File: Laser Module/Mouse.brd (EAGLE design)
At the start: 100 x 50 mm, 74 parts, among them Q2 2.5A/30V, U1 RFM69HCW, U10 74AHC1G125, U2 HALL-EFFECTSMD, U3 HALL-EFFECTSMD, U4 HALL-EFFECTSMD, U5 HALL-EFFECTSMD, U6 BQ27441-G1, U7 BQ24075, U8 ATSAMD21G-A, U9 3.3V, Y1 32.768kHz

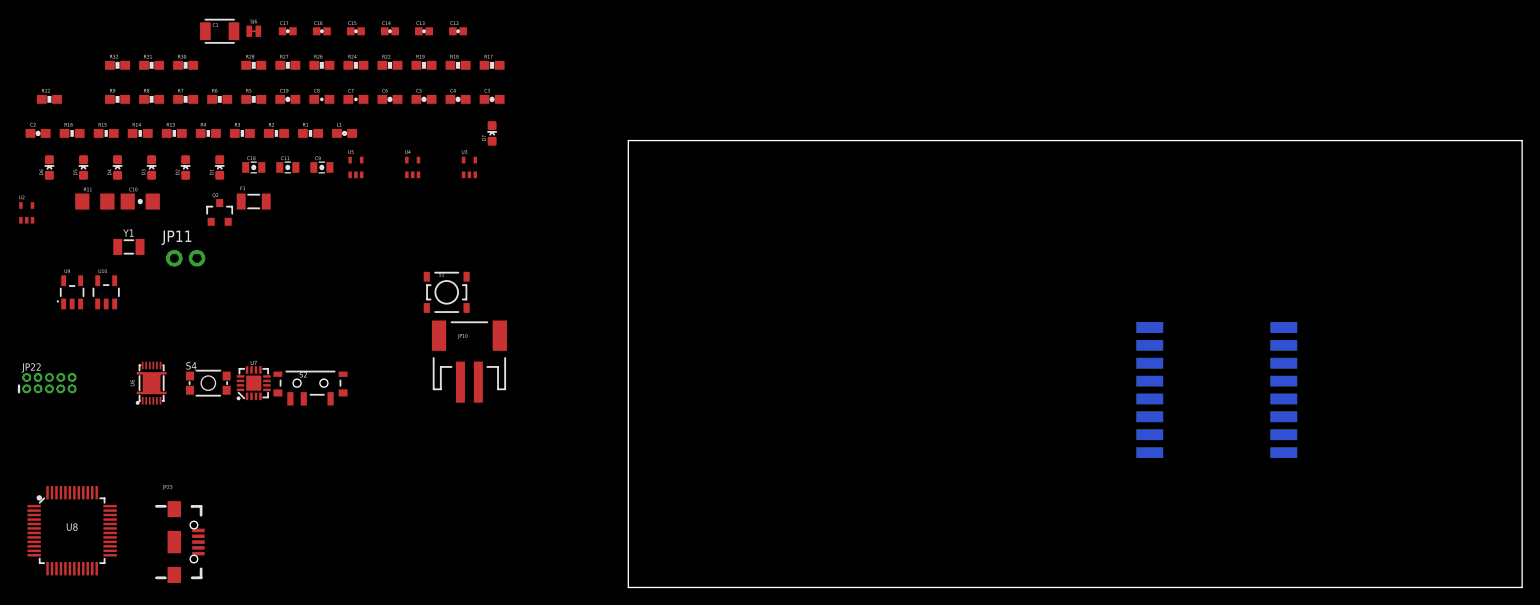
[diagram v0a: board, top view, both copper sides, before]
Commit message: Worked on the laser and dongle schematics Placed the parts on the laser and dongle boards in their rough locations
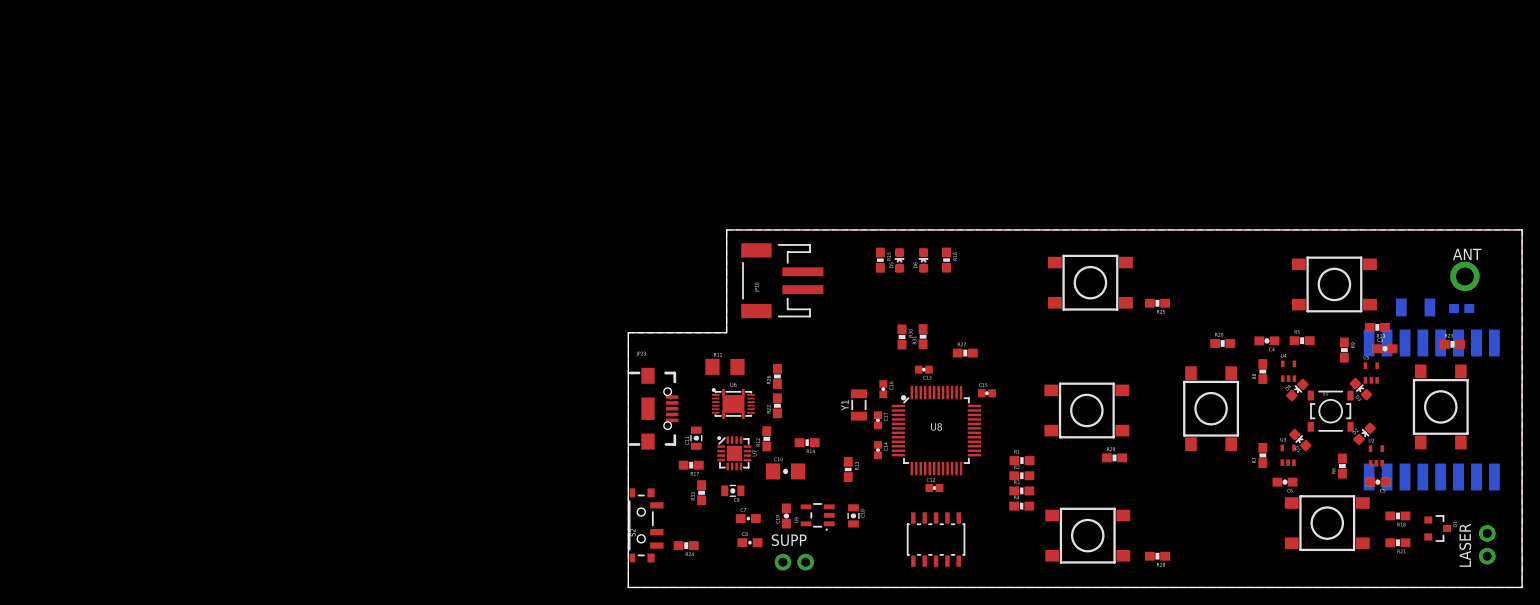
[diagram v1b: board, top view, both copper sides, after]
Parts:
- removed D7: RED, SparkFun-LED:LED-0603
- removed F1: 500mA, SparkFun-PowerIC:PTC-1206
- removed JP11: (no value), mike-temp:1X02_NO_SILK
- removed L1: FB - 30Ohm, SparkFun-Passives:0603
- removed Q2: 2.5A/30V, SparkFun-DiscreteSemi:SOT23-3
- removed R19: 10K, SparkFun-Resistors:0603-RES
- removed R32: 47K, SparkFun-Resistors:0603-RES
- removed SJ6: PWR-LED, SparkFun-Passives:PAD-JUMPER-2-NC_BY_TRACE_NO_SILK
- removed U10: 74AHC1G125, SparkFun-DigitalIC:SOT23-5
- added ANT: (no value), SparkFun-Connectors:1X01_2MM
- added LASER: (no value), SparkFun-Connectors:1X02_NO_SILK
- added Q1: MOSFET-NCHANNELAO3404A, SparkFun-DiscreteSemi:SOT23-3
- added R10, R20, R21, R23, R25, R29: 10k, SparkFun-Resistors:0603-RES
- added R33: 10K, SparkFun-Resistors:0603-RES
- added S3, S5, S6, S7, S8, S9: SWITCH-MOMENTARY-2SMD-4, SparkFun-Electromechanical:TACTILE_SWITCH_TALL
- added SUPP: (no value), mike-temp:1X02_NO_SILK
- JP22: value CORTEX_DEBUGPTH -> CORTEX_DEBUGSMD; device samd21-temp:2X5-PTH-1.27MM -> SparkFun-Connectors:SAMTECH_FTSH-105-01
- R18: value 10K -> 330
- R28: value 330 -> 10k
- S4: value RESET -> SWITCH-MOMENTARY-2SMD-4; device samd21-temp:TACTILE_SWITCH_SMD_4.6X2.8MM -> SparkFun-Electromechanical:TACTILE_SWITCH_TALL
- moved C2 160.5 mm to (93.2, 31.2), flipped to the bottom, turned to 180 degrees
- moved U2 153.4 mm to (83.7, 14.7)
- moved R9 140.1 mm to (80.1, 26.6), turned to 270 degrees
- moved D3 137.6 mm to (82.0, 22.2), turned to 45 degrees
- moved C1 137.3 mm to (88.1, 31.3), flipped to the bottom
- moved D2 135.2 mm to (82.4, 17.2), turned to 315 degrees
- moved D4 134.3 mm to (74.8, 22.1), turned to 315 degrees
- moved R6 132.1 mm to (79.9, 13.6), turned to 90 degrees
- moved R8 128.0 mm to (71.0, 24.2), turned to 90 degrees
- moved R7 126.9 mm to (71.0, 14.8), turned to 90 degrees
- moved D1 124.7 mm to (75.2, 16.5), turned to 45 degrees
- moved R5 120.4 mm to (75.4, 27.6)
- moved R18 116.6 mm to (86.1, 8.00), turned to 180 degrees
- moved U5 115.9 mm to (83.1, 24.0)
- moved R28 115.1 mm to (59.2, 3.50), turned to 180 degrees
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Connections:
- removed net A0: U8.3
- removed net A1: U8.7
- removed net A2: U8.8
- removed net A3: U8.9
- removed net AREF: U8.4
- removed net D0/RXI: U8.16
- removed net D1/TXO: U8.15
- removed net D10/SS: U8.27
- removed net D11/MOSI: U8.25
- removed net D12/MISO: U8.28
- removed net D13/SCK: U8.26
- removed net D2: U8.23
- removed net D3: U8.14
- removed net D4: U8.13
- removed net D5: U8.24
- removed net D6: U8.29
- removed net D7: U8.30
- removed net D8: U8.11
- removed net D9: U8.12
- removed net EN2: U7.5
- removed net N$14: D7.A, R28.1
- removed net N$18: F1.2, Q2.3
- removed net N$20: Q2.1, R32.1, U10.4
- removed net N$23: D7.C, SJ6.2
- removed net RF_NSS: U1.5
- removed net RX_LED: U8.48
- removed net SCL: U8.32
- removed net SDA: U8.31
- removed net TRK_BTN: R5.2, S1.1
- removed net TX_LED: U8.39
- new net DWN_BTN: R23.2, S6.A2, U8.15
- new net LFT_BTN: R10.2, S3.A2, U8.8
- new net LFT_MOUSE: R28.2, S8.A2, U8.21
- new net LSR_BTN: R25.2, S7.A2, U8.16
- new net LSR_OUT: R18.2, U8.9
- new net MDL_MOUSE: R5.2, S1.1, U8.11
- new net N$6: Q1.1, R18.1
- new net N$8: LASER.2, Q1.3
- new net RF_SS: U1.5, U8.27
- new net RHT_BTN: R21.2, S5.A2, U8.14
- new net RHT_MOUSE: R29.2, S9.A2, U8.22
- new net UP_BTN: R20.2, S4.A2, U8.13
- net !RESET: no longer S4.3, S4.4
- net 3.3V: now also S3.B2, S4.B2, S5.B2, S6.B2, S7.B2, S8.B2, S9.B2; no longer L1.1, R28.2
- net ANT: now also ANT.1
- net BLU_PWM: now also U8.23
- net BMS_SCL: now also U8.32
- net BMS_SDA: now also U8.31
- net EN1: now also R33.2; no longer R18.2
- net GND: now also Q1.2, R10.1, R20.1, R21.1, R23.1, R25.1, R28.1, R29.1, SUPP.2, U7.5; no longer JP11.2, R19.2, S4.1, S4.2, SJ6.1, U10.3
- net GPOUT: now also U8.10
- net GRN_PWM: now also U8.29
- net HALL_DWN: now also U8.47
- net HALL_LFT: now also U8.48
- net HALL_RHT: now also U8.7
- net HALL_UP: now also U8.12
- net N$19: no longer U10.1, U10.2
- net OUT: now also R33.1; no longer R18.1, R19.1
- net RED_PWM: now also U8.24
- net RF_MISO: now also U8.28
- net RF_MOSI: now also U8.25
- net RF_SCK: now also U8.26
- net VDDANA: no longer L1.2
- net VIN: no longer Q2.2, R32.2, U10.5
- net V_BATT: now also LASER.1
- net V_USB: now also SUPP.1; no longer F1.1, JP11.1
- net WHT_PWM: now also U8.30
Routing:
- added copper zone on layer 1, net GND
- added copper zone on layer 16, net GND
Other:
- board size 100 x 50 mm -> 100 x 40 mm

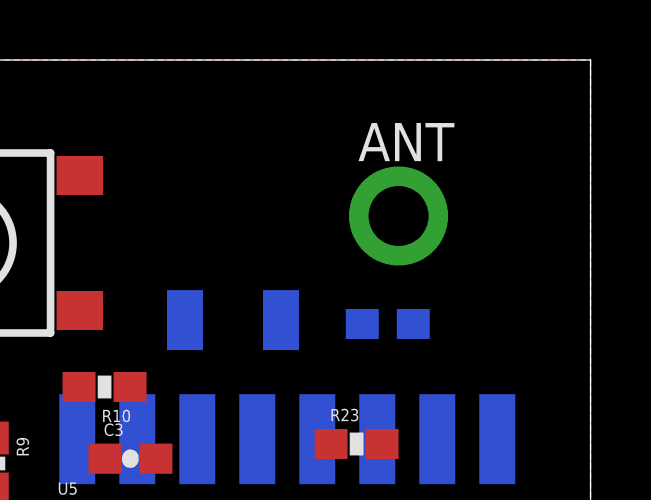
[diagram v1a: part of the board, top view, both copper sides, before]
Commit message: Created, placed, and routed a starter board for the Camera Module
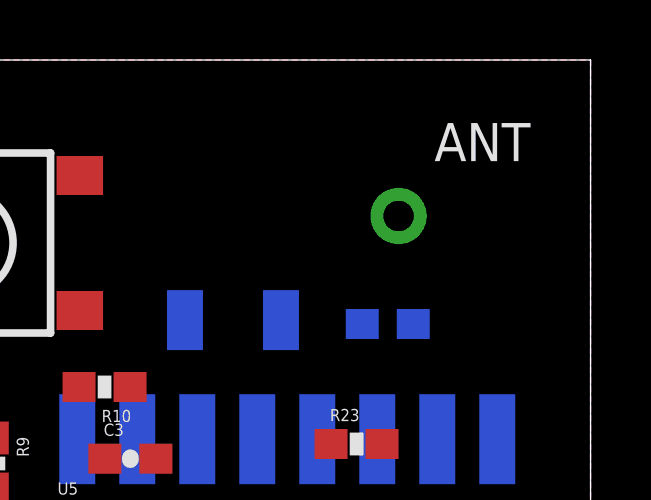
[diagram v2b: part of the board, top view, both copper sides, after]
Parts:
- ANT: device SparkFun-Connectors:1X01_2MM -> SparkFun-Connectors:1X01_NO_SILK
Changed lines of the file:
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@@
 <attribute name="PROD_ID" value="RES-00824" x="8.2" y="10.6" size="1.778" layer="27" rot="R90" display="off"/>
 </element>
-<element name="ANT" library="SparkFun-Connectors" package="1X01_2MM" value="" x="93.6" y="34.8"/>
+<element name="ANT" library="SparkFun-Connectors" package="1X01_NO_SILK" value="" x="93.6" y="34.8"/>
 <element name="Q1" library="SparkFun-DiscreteSemi" package="SOT23-3" value="MOSFET-NCHANNELAO3404A" x="90.5" y="6.6" smashed="yes" rot="R270">
 <attribute name="PROD_ID" value="TRAN-12988" x="90.5" y="6.6" size="1.778" layer="27" rot="R270" display="off"/>

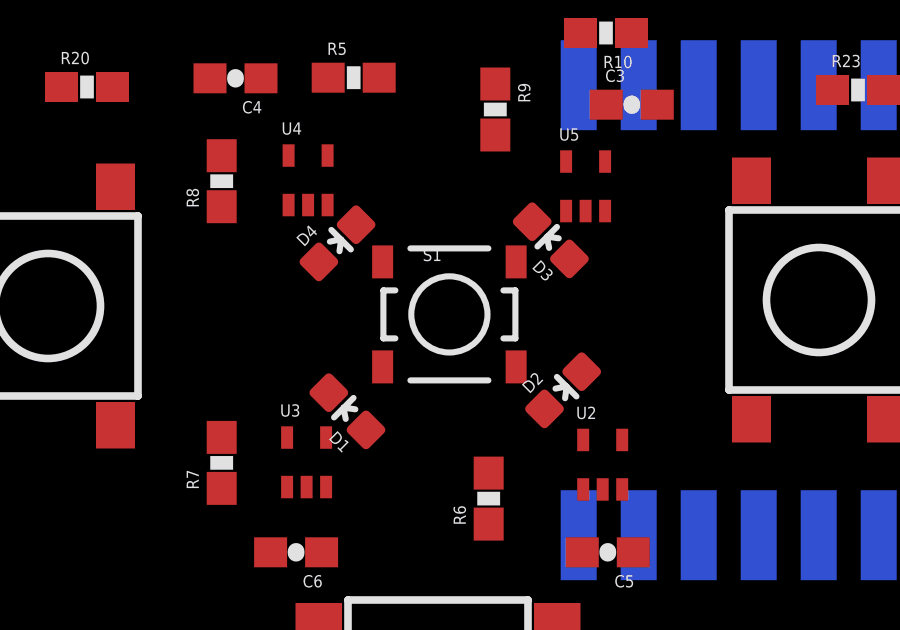
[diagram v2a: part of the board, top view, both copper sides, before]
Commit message: Routed the dongle and camera modules
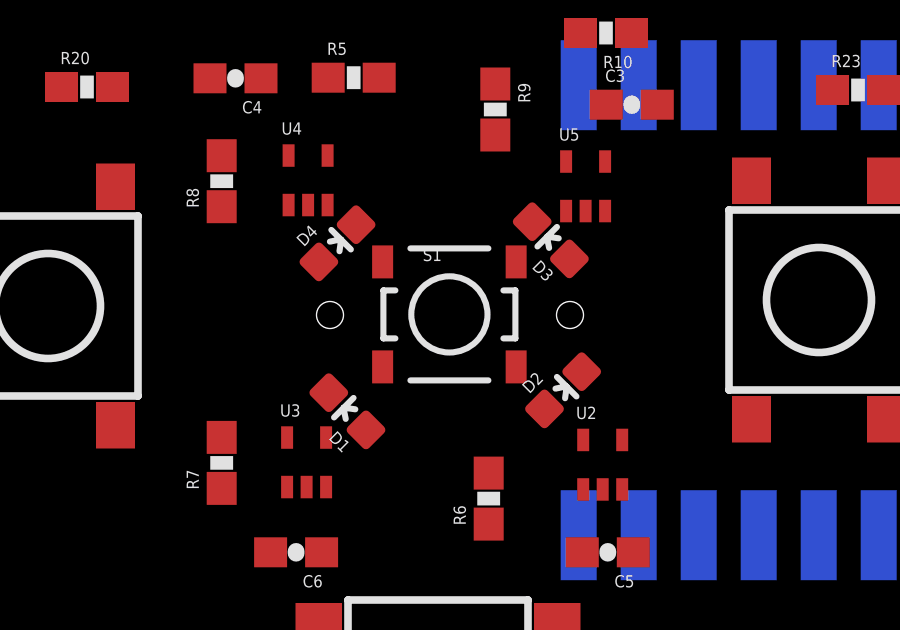
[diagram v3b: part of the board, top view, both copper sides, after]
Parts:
- added U$1: TRACKBALLMECH, SparkFun-Electromechanical:TRACKBALL
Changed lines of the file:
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@@
 </element>
 <element name="LASER" library="SparkFun-Connectors" package="1X02_NO_SILK" value="" x="96.1" y="3.5" rot="R90"/>
+<element name="U$1" library="SparkFun-Electromechanical" package="TRACKBALL" value="TRACKBALLMECH" x="78.6" y="19.7">
+<attribute name="PROD_ID" value="COMP-09237" x="78.6" y="19.7" size="1.778" layer="27" display="off"/>
+</element>
 </elements>
 <signals>

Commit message: Updated the RFM69 library to be closer to C. millis() is the only function hat needs to be updated now.
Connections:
- new net RF_INT: U1.14, U8.4
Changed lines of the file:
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@@
 <wire x1="91.6" y1="6.6" x2="96.1" y2="6.04" width="0" layer="19" extent="1-1"/>
+</signal>
+<signal name="RF_INT">
+<contactref element="U1" pad="14"/>
+<contactref element="U8" pad="4"/>
+<wire x1="30.22" y1="18.8" x2="92.89" y2="27.36" width="0" layer="19" extent="1-16"/>
 </signal>
 </signals>

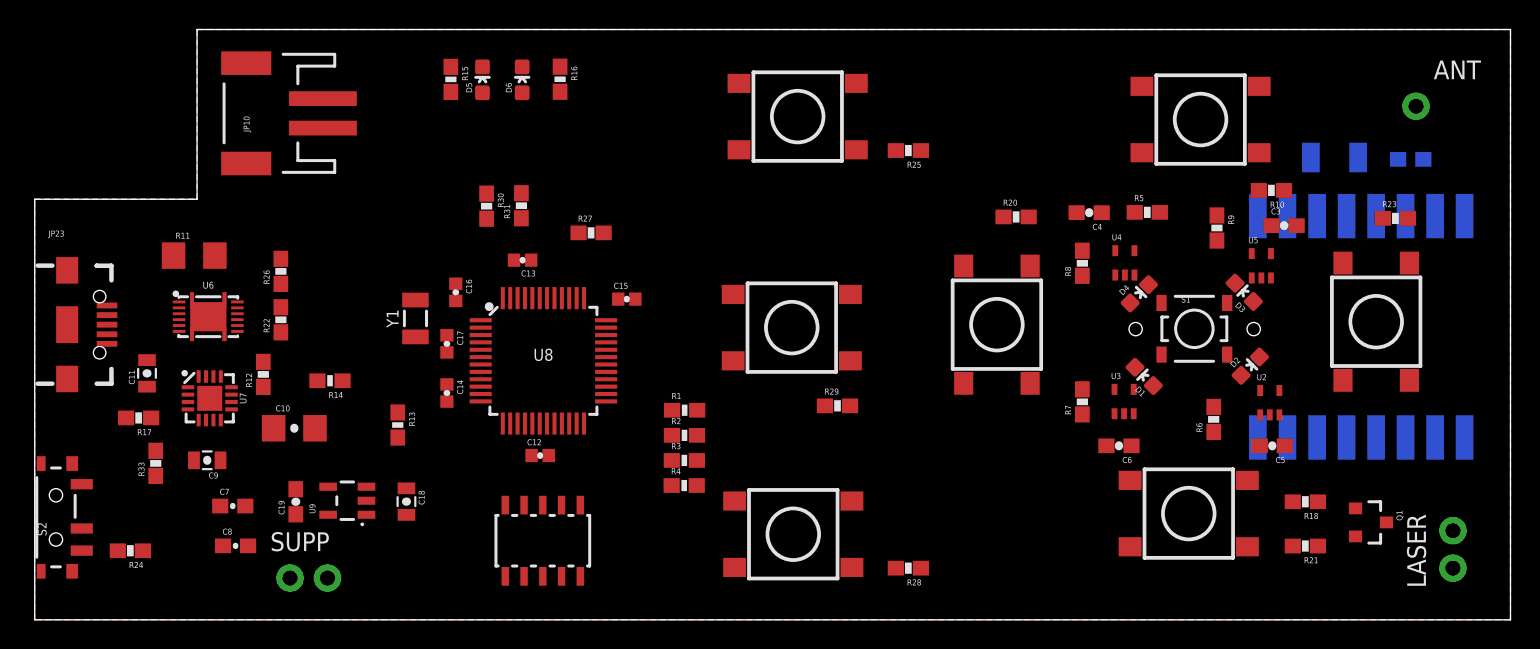
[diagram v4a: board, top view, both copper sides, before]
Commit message: Started the routing of the laser module board Updated the Dongle Module C project to allow for absolute mouse control
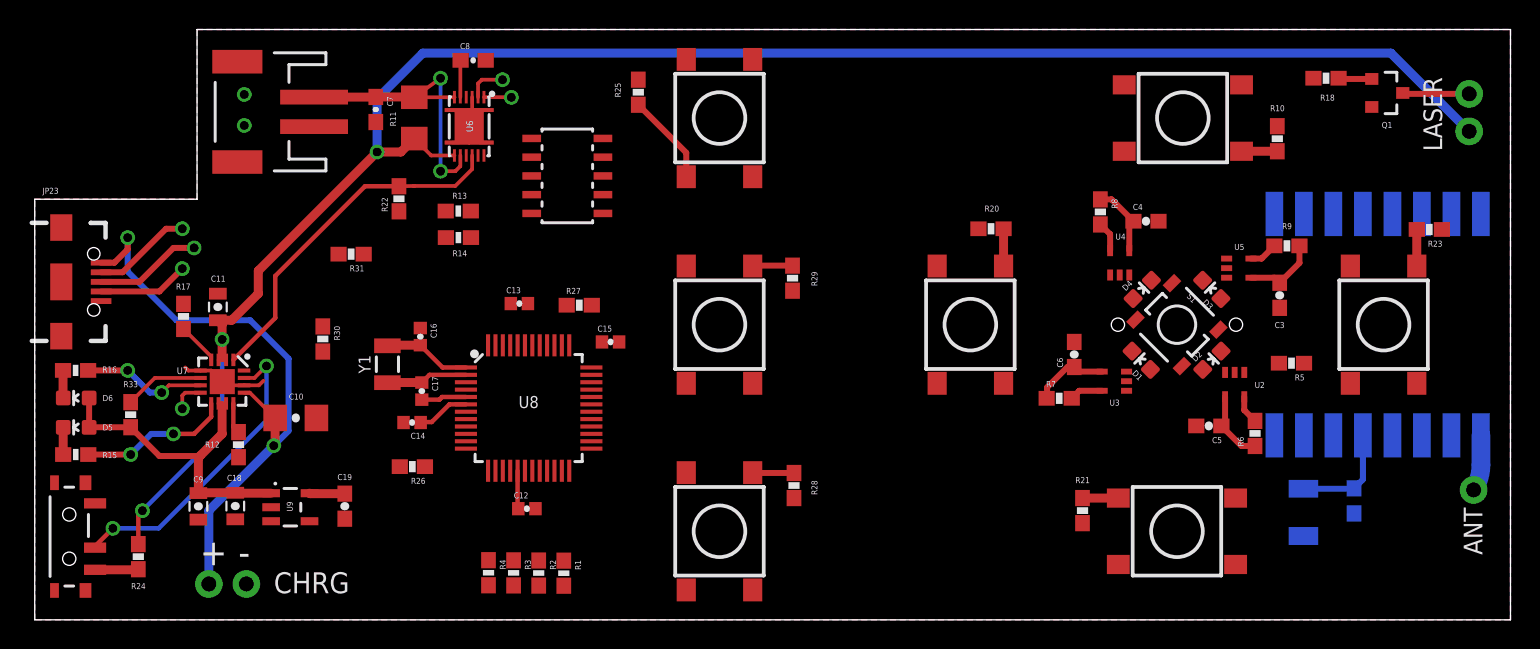
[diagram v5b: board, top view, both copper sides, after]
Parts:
- moved R16 38.3 mm to (2.77, 16.9), turned to 0 degrees
- moved D6 37.1 mm to (2.81, 15.0), turned to 90 degrees
- moved C8 36.6 mm to (29.7, 37.9)
- moved D5 36.2 mm to (2.81, 13.0), turned to 90 degrees
- moved R15 35.9 mm to (2.78, 11.2), turned to 0 degrees
- moved LASER 29.6 mm to (97.2, 33.1)
- moved Q1 29.1 mm to (91.6, 35.7)
- moved R18 28.7 mm to (87.5, 36.7)
- moved C7 28.6 mm to (23.1, 34.6), turned to 270 degrees
- moved ANT 26.3 mm to (97.5, 8.80), turned to 180 degrees
- moved JP22 24.8 mm to (36.1, 30.1), turned to 90 degrees
- moved C1 24.1 mm to (86.0, 7.28), turned to 270 degrees
- moved C2 23.5 mm to (89.4, 8.06), turned to 270 degrees
- moved U6 21.9 mm to (29.4, 33.4), turned to 180 degrees
- moved R25 18.7 mm to (40.9, 35.8), turned to 270 degrees
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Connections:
- removed net VCC: C3.1, C4.1, C5.1, C6.1, R5.1, R6.1, R7.1, R8.1, R9.1, U2.4, U3.4, U4.4, U5.4
- removed net VIN: C18.1, R30.2, U9.1, U9.3
- net 3.3V: now also C3.1, C4.1, C5.1, C6.1, R5.1, R6.1, R7.1, R8.1, R9.1, U2.4, U3.4, U4.4, U5.4
- net OUT: now also C18.1, R30.2, U9.1, U9.3
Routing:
- net V_BATT: track 0.00 -> 123.1 mm, vias 0 -> 3
- net V_USB: track 0.00 -> 40.9 mm, vias 0 -> 2
- net 3.3V: track 0.00 -> 32.5 mm
- net TS: track 0.00 -> 24.1 mm
- net OUT: track 0.00 -> 22.7 mm
- net GND: track 0.00 -> 21.0 mm, vias 0 -> 3
- net SYSOFF: track 0.00 -> 20.8 mm, vias 0 -> 2
- net BATTERY_IN: track 0.00 -> 20.2 mm, vias 0 -> 2
- net !CHG!: track 0.00 -> 10.3 mm, vias 0 -> 2
- net !PGOOD!: track 0.00 -> 8.44 mm, vias 0 -> 2
- net USB_D+: track 0.00 -> 7.25 mm, vias 0 -> 1
- net USB_D-: track 0.00 -> 6.72 mm, vias 0 -> 1
- net LSR_BTN: track 0.00 -> 6.22 mm
- net N$19: track 0.00 -> 6.14 mm, vias 0 -> 1
- net N$10: track 0.00 -> 5.96 mm
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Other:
- board text added: "+"
- board text added: "-"
- board text added: "CHRG"
